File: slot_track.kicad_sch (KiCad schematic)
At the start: 37 parts, among them J1 Barrel_Jack_Switch, J2 SWD Debug, T1 LinearTouch4, T2 Conn_01x01, T3 LinearTouch4, U1 STM32F051C6Tx, U2 MCP1754S-3302xCB, U3 ZXBM5210-SP, U4 ZXBM5210-SP, U5 ZXBM5210-SP

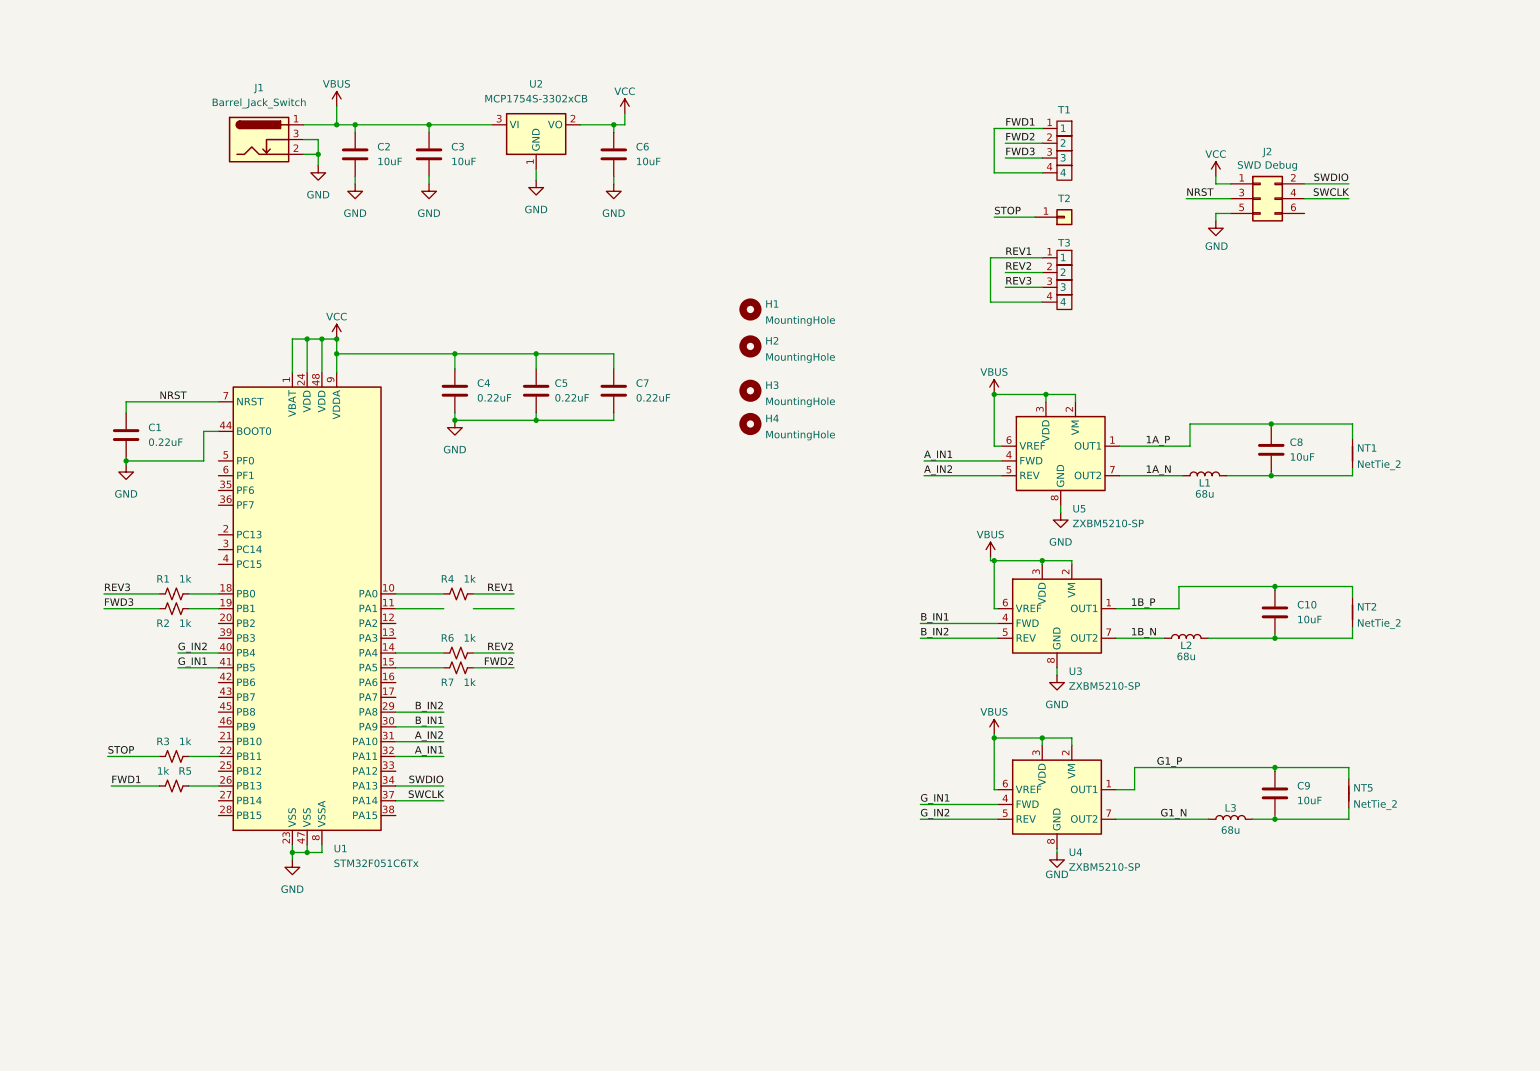
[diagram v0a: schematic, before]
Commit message: Rev 2
- Adjusts track shape
- Swaps guard rails to top and phase to In1. Hopefully this lowers the
noise and friction.
- Adds sample caps
- Adds SWCLK resistor
- Adds divider for Vin measurement
- Switches to a PH connector for SWD and a UART
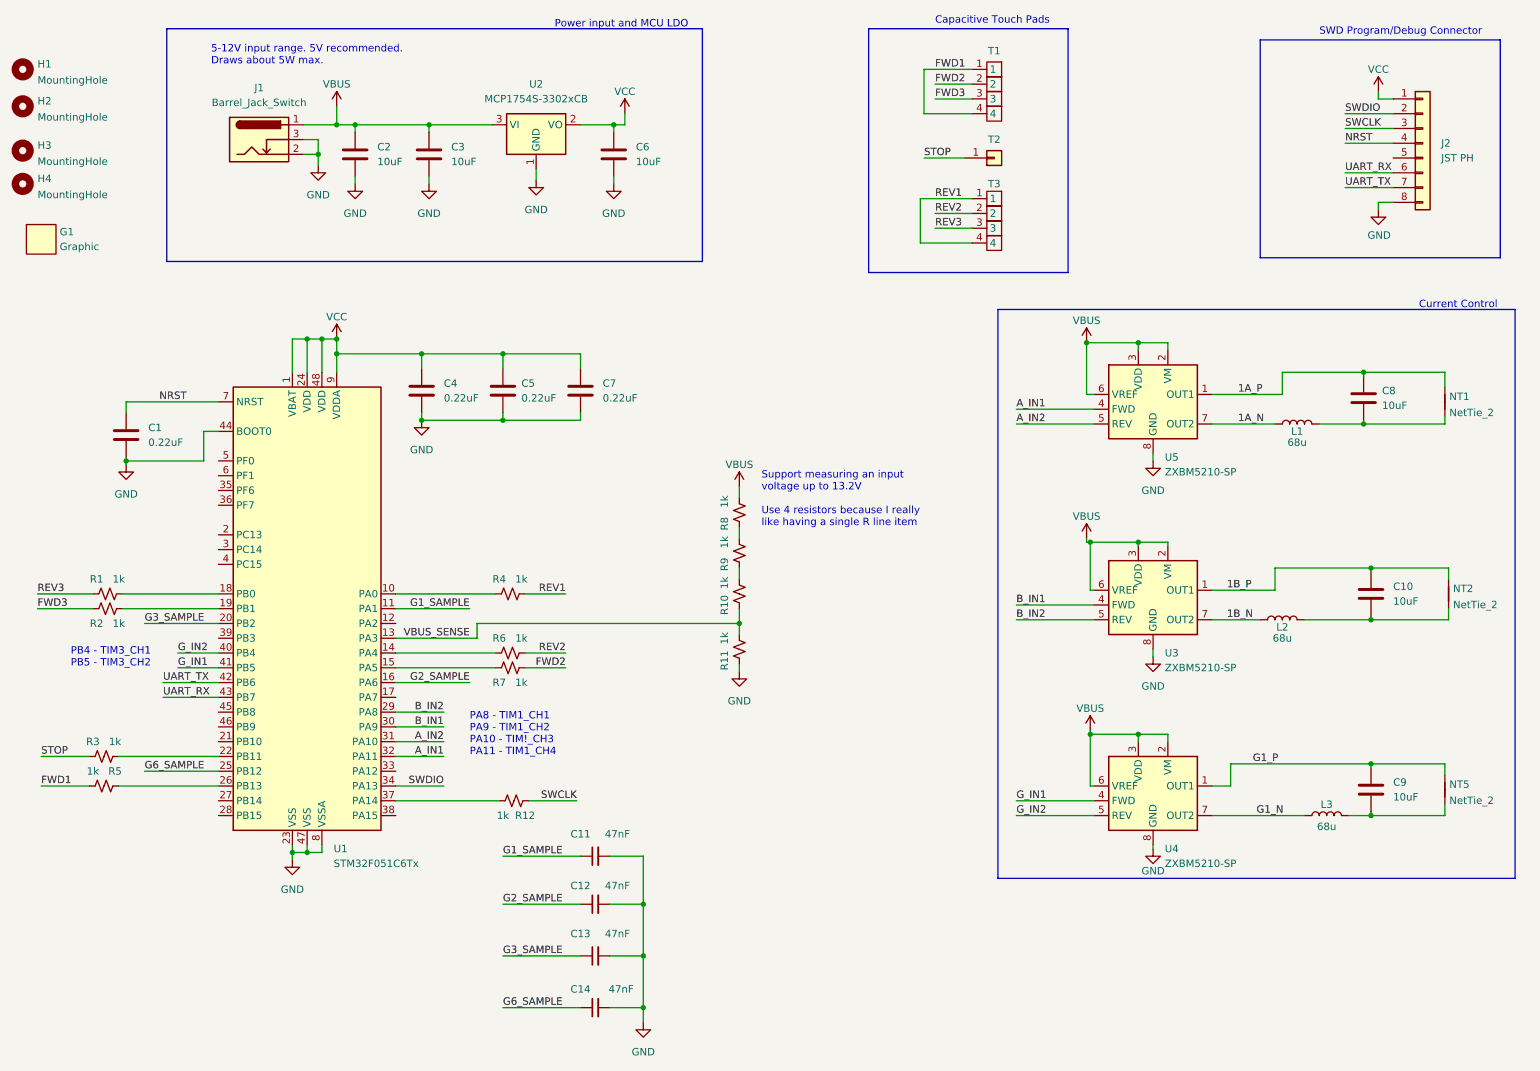
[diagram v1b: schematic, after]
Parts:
- removed J2: SWD Debug, Connector_PinHeader_2.54mm:PinHeader_2x03_P2.54mm_Vertical_SMD, symbol Connector_Generic:Conn_02x03_Odd_Even
- added C11, C12, C13, C14: 47nF, Capacitor_SMD:C_0603_1608Metric, symbol Device:C_Small
- added G1: Graphic, track:magnetlogo, symbol track_v2:Graphic
- added J2: JST PH, Connector_JST:JST_PH_S8B-PH-SM4-TB_1x08-1MP_P2.00mm_Horizontal, symbol Connector_Generic:Conn_01x08
- added R10, R11, R12, R8, R9: 1k, Resistor_SMD:R_0603_1608Metric, symbol Device:R_Small_US
- H1, H2, H3, H4: footprint MountingHole:MountingHole_3.2mm_M3 -> MountingHole:MountingHole_3.5mm; Config (none) -> Not Fitted
- J1: Part Description (none) -> CONN PWR JACK 2X5.5MM SOLDER
- L1, L2, L3: Part Description (none) -> FIXED IND 68UH 2.1A 110 MOHM SMD
- NT1, NT2, NT5, T1, T2, T3: Config (none) -> Not Fitted
- R1, R2, R3, R4, R5, R6, R7: Mfg Part Number (none) -> AC0603JR-101KL; Part Description (none) -> RES 1k 0603 +/- 5% 0.1W Thick Film
- U1: Mfg Part Number (none) -> STM32F051C6T7; Part Description (none) -> IC MCU 32BIT 32KB FLASH 48LQFP
- U2: Part Description (none) -> IC REG LIN 3.3V 150MA SOT23A-3
- U3, U4, U5: Part Description (none) -> IC MOTOR DRIVER 3V-18V 8SO
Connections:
- net GND: now also C11.2, C12.2, C13.2, C14.2, J2.8 (Pin_8), R11.1
- net NRST: now also J2.4 (Pin_4)
- net SWCLK: now also J2.3 (Pin_3), R12.1; no longer U1.37 (PA14)
- net SWDIO: now also J2.2 (Pin_2)
- net VBUS: now also R8.2
- net VCC: now also J2.1 (Pin_1)
- net G1_SAMPLE: now reaches U1.11 (PA1)
- net G1_SAMPLE: now also C11.1
- net VBUS_SENSE: now reaches U1.13 (PA3)
- net VBUS_SENSE: now also R10.1, R11.2
- net G2_SAMPLE: now reaches U1.16 (PA6)
- net G2_SAMPLE: now also C12.1
- net G3_SAMPLE: now reaches U1.20 (PB2)
- net G3_SAMPLE: now also C13.1
- net G6_SAMPLE: now reaches U1.25 (PB12)
- net G6_SAMPLE: now also C14.1
- net UART_TX: now reaches U1.42 (PB6)
- net UART_TX: now also J2.7 (Pin_7)
- net UART_RX: now reaches U1.43 (PB7)
- net UART_RX: now also J2.6 (Pin_6)
- new net: R12.2, U1.37 (PA14)
- new net: R10.2, R9.1
- new net: R8.1, R9.2
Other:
- note added: "5-12V input range. 5V recommended. Draws about 5W max."
- note added: "Capacitive Touch Pads"
- note added: "Current Control"
- note added: "PA8 - TIM1_CH1 PA9 - TIM1_CH2 PA10 - TIM!_CH3 PA11 - TIM1_CH4"
- note added: "PB4 - TIM3_CH1 PB5 - TIM3_CH2"
- note added: "Power input and MCU LDO"
- note added: "SWD Program/Debug Connector"
- note added: "Support measuring an input voltage up to 13.2V Use 4 resistors because I really like having a single R line item"
- company: (none) -> Relative Jump Labs
- title: (none) -> Gauss Speedway
- moved on the sheet: C10, C4, C5, C7, C8, C9, H1, H2, H3, H4, L1, L2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
